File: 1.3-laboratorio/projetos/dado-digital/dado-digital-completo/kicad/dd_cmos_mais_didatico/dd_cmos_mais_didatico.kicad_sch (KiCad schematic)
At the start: 50 parts, among them J1 Conn_01x02, J2 Conn_01x02, J3 Conn_01x01, J4 Conn_01x01, J5 Conn_01x02, Q1 BC547, SW1 SW_PUSH, U1 4093, U2 4027, U3 4518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

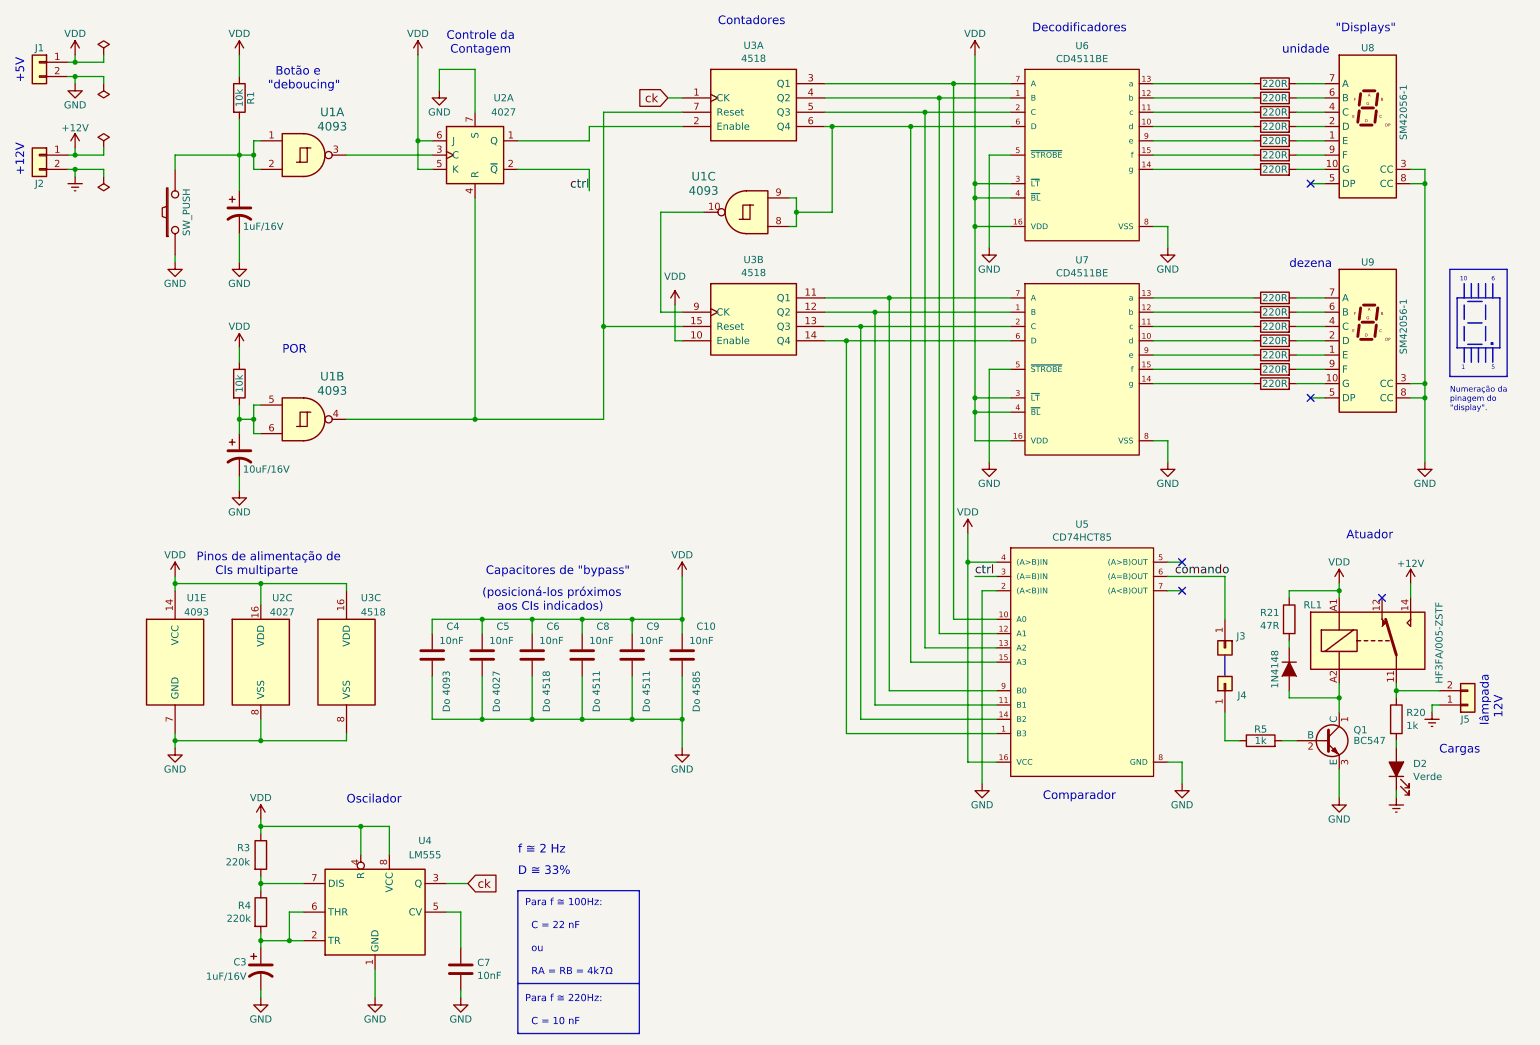
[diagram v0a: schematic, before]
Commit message: dd_cmos_mais_didatico: máscara de igualdade por meio de porta lógica e alteração de transistor NPN para PNP; no final, utilizaram-se duas portas lógicas a mais, mas foi possível manter a mesma quantidade de CIs. As alterações foram envidadas para avaliação. Está na pendência o ensaio prático.
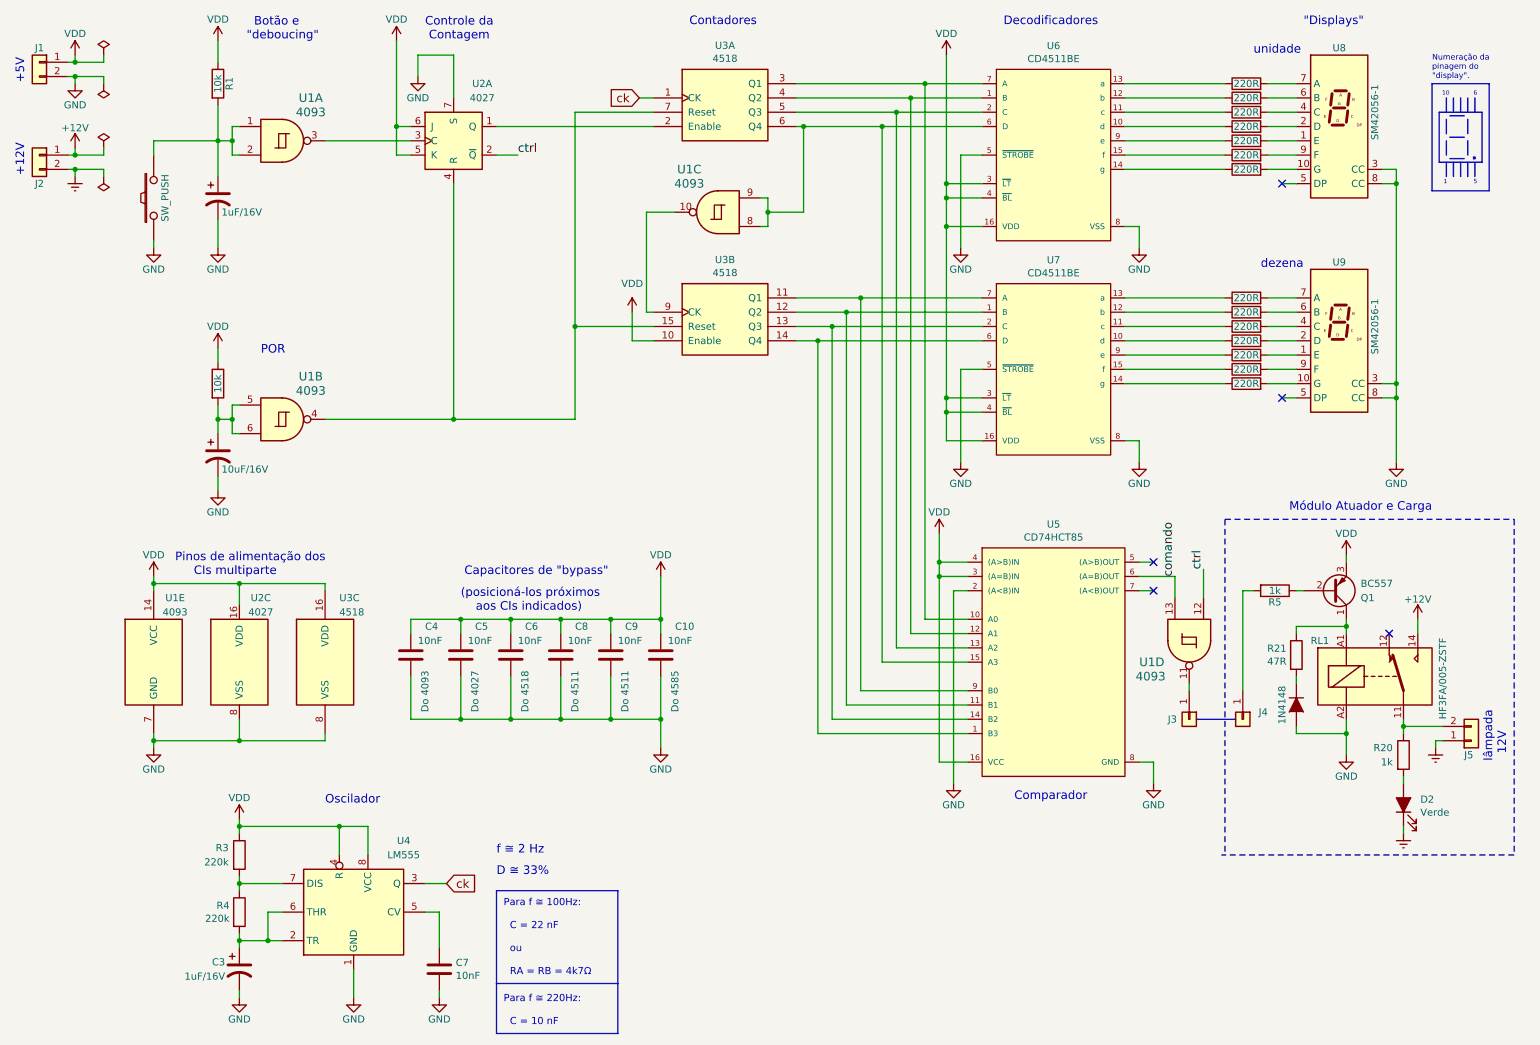
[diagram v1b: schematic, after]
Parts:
- removed Q1: BC547, Package_TO_SOT_THT:TO-92, symbol DD_CMOS-rescue:BC549
- added Q1: BC557, Package_TO_SOT_THT:TO-92_Inline, symbol Transistor_BJT:BC557
- added unit 4 of U1
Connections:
- net GND: now also D1.2 (A), RL1.A2
- net VDD: now also U5.3 ((A=B)IN), Q1.3 (E); no longer R21.1, RL1.A1
- net comando: now also U1.13; no longer J3.1 (Pin_1)
- net ctrl: now also U1.12; no longer U5.3 ((A=B)IN)
- net at R5.1: now also Q1.2 (B); no longer J4.1 (Pin_1)
- net at R5.2: now also J4.1 (Pin_1)
- new net: Q1.1 (C), R21.1, RL1.A1
- new net: J3.1 (Pin_1), U1.11
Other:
- note added: "Módulo Atuador e Carga"
- note added: "Pinos de alimentação dos CIs multiparte"
- note removed: "Atuador"
- note removed: "Cargas"
- note removed: "Pinos de alimentação de CIs multiparte"
- moved on the sheet: C10, C3, C4, C5, C6, C7, C8, C9, D2, J3, J4, J5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
